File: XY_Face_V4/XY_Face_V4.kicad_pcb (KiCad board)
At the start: 4 copper layers, 83 x 98 mm, 38 parts, among them CN1 DF11-2DSA-4DP, J11 DF11-4DP-2DSA, J13 DF11-4DP-2DSA, J2 Conn_01x01, J3 Conn_01x01, J4 Conn_01x01, J5 Conn_01x01, Q2 CSD17576Q5B, U1 VEML7700, U2 TMP112xxDRL, U3 DRV2605LDGS, U4 TCA4311ADGKR, U5 5040500691, U6 5040500691

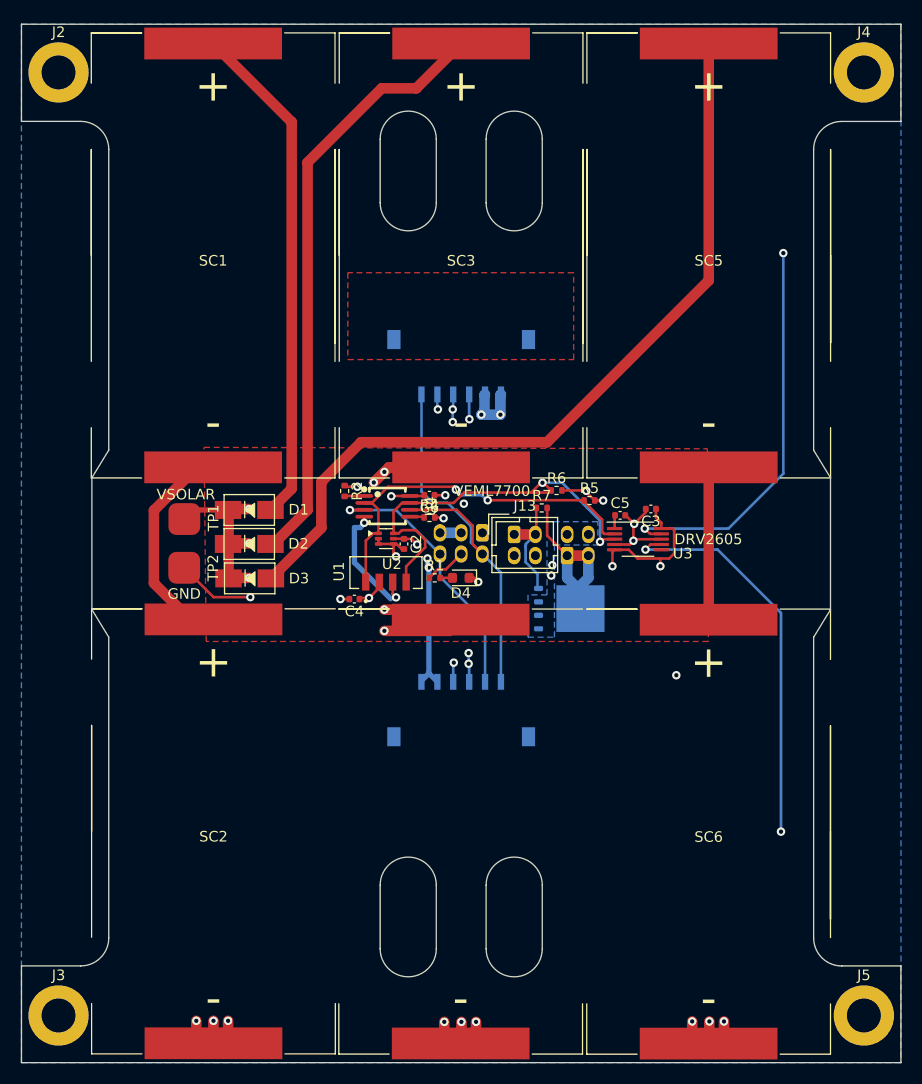
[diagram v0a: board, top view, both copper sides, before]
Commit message: Removed 2p Solar Cells
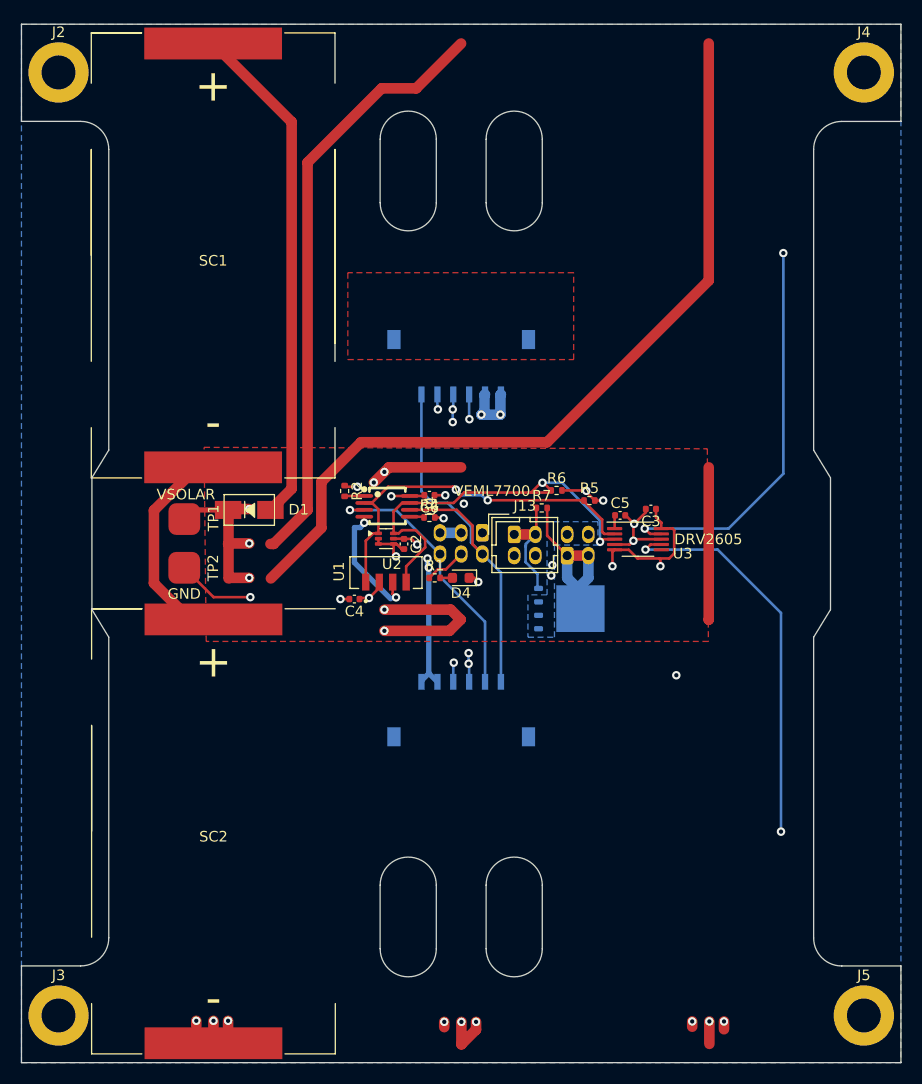
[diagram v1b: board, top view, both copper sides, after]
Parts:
- removed D2, D3: CDBA240LL-HF, SolarPanelBoards:DO-214AC
- removed SC3, SC4, SC5, SC6: SM101K07TF, SolarPanelBoards:KXOB101K08F-TR

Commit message: V4: Added new Cells to Footprint
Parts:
- removed U1: VEML7700, VEML7700-TT:XDCR_VEML7700-TT
- added U7: VEML6031X00, easyeda2kicad:SENSOR-SMD_VEML6031X00, F.Cu at (130.5, 116.0)
- SC1, SC2: value SM101K07TF -> SM261K10TF; footprint SolarPanelBoards:KXOB101K08F-TR -> Solar_Cell_Library:SM261K10TF
- moved SC1 23.4 mm to (144.4, 88.5), turned to 180 degrees
- moved SC2 23.3 mm to (144.4, 141.0), turned to 180 degrees
- moved U2 6.81 mm to (130.7, 113.0)
- moved C2 6.73 mm to (132.5, 113.5)
- moved TP1 4.40 mm to (114.0, 113.0)
- moved TP2 4.39 mm to (114.0, 116.5)
- moved C4 3.53 mm to (134.0, 116.5)
- moved D1 3.41 mm to (124.5, 115.0), turned to 180 degrees
- moved R7 2.96 mm to (155.0, 112.0)
- moved C3 0.50 mm to (162.4, 112.0)
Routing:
- net Net-(D3-A): track 77.9 -> 0.00 mm
- net Net-(SC1--): track 21.2 -> 82.5 mm
- net Net-(D2-A): track 56.8 -> 0.00 mm
- net Net-(SC3--): track 39.9 -> 0.00 mm, vias 4 -> 0
- net GND: track 53.5 -> 26.9 mm, vias 21 -> 9
- net Net-(D1-A): track 47.9 -> 26.5 mm
- net Net-(SC5--): track 14.4 -> 0.00 mm
- net /SDA: track 39.0 -> 28.7 mm
- net VSOLAR: track 87.5 -> 77.6 mm, vias 7 -> 4
- net /SCL: track 36.0 -> 28.4 mm
- net Net-(J13-Pin_1): track 10.5 -> 11.8 mm
- net /RBF_High: track 18.1 -> 17.1 mm
- net +3V3: track 105.9 -> 105.3 mm, vias 13 -> 12
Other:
- board text removed: "VEML7700"

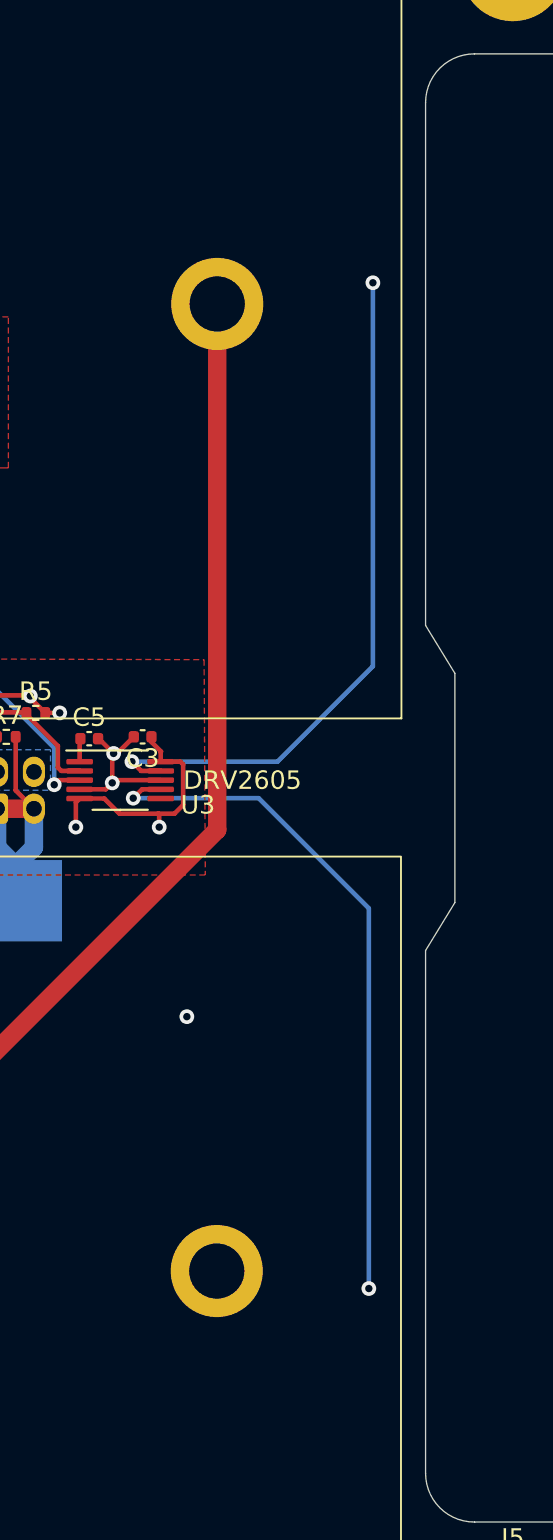
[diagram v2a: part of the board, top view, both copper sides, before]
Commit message: V4: Fixed In1 Coils
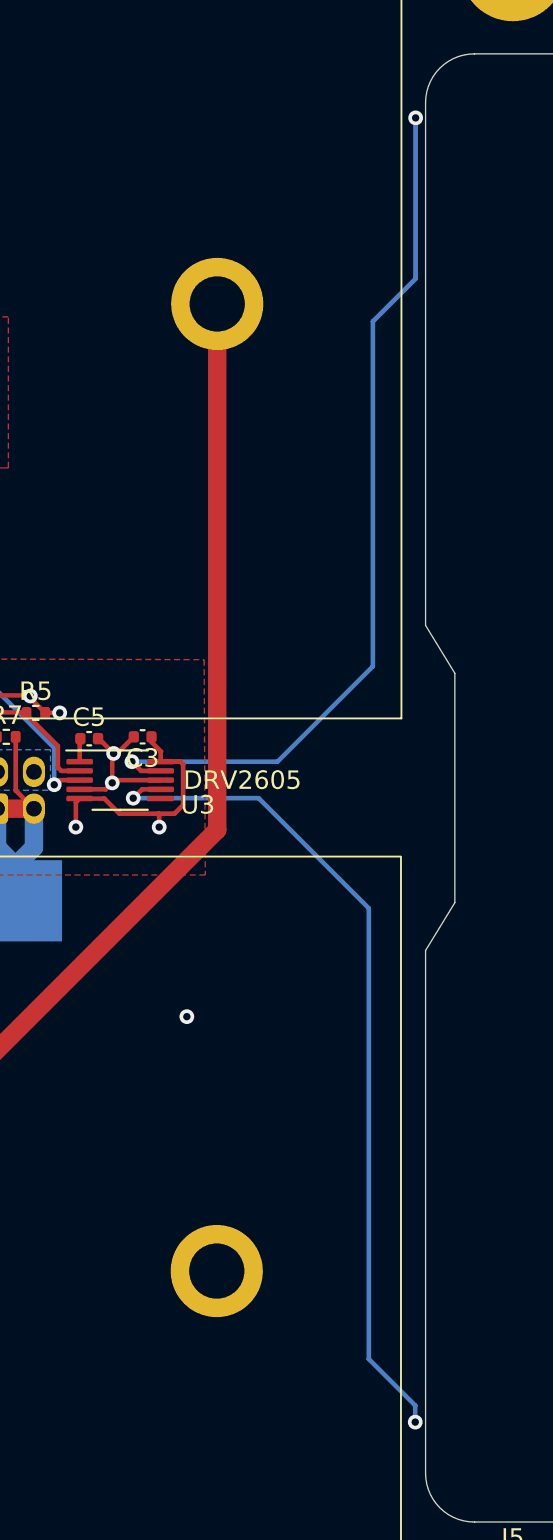
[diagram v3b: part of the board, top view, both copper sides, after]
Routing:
- net Net-(U3-OUT+): track 9246.2 -> 9743.8 mm

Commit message: V4: Completed Redraw of Traces
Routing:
- net Net-(U3-OUT+): track 9743.8 -> 10520.8 mm

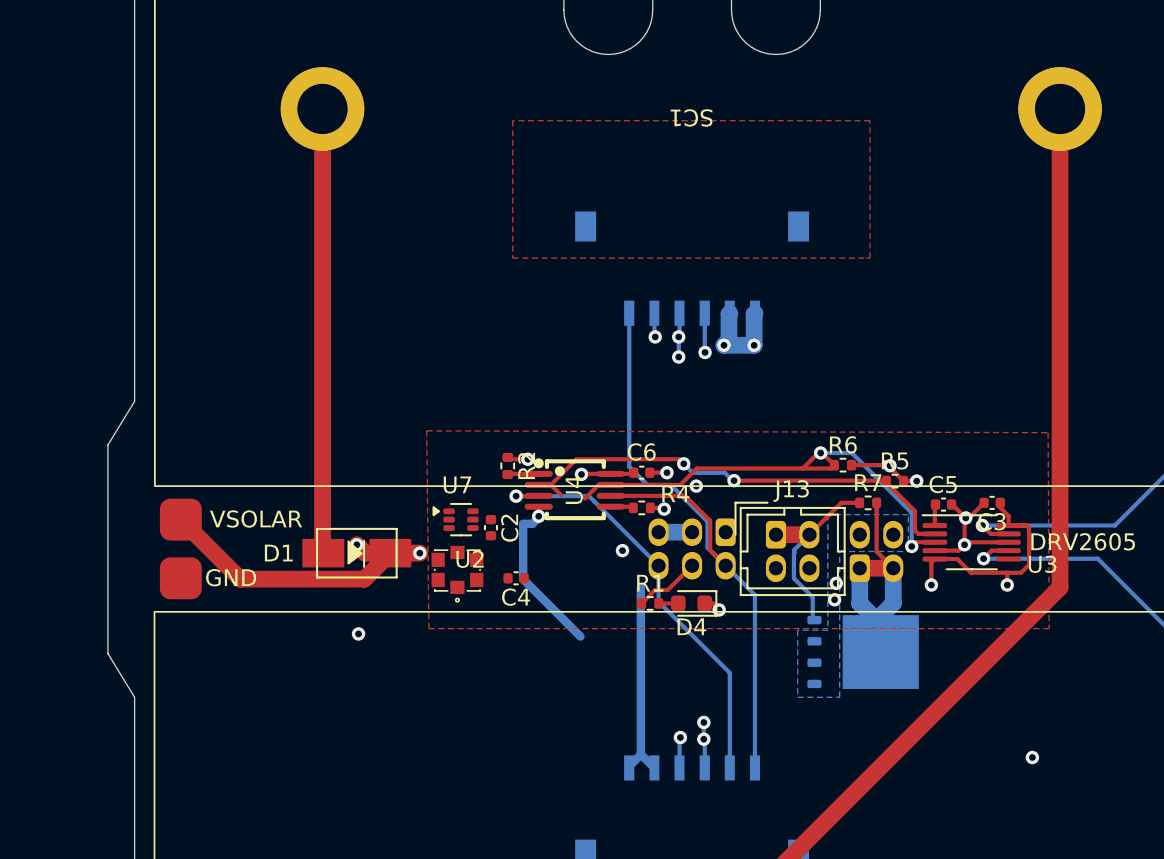
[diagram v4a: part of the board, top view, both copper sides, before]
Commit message: V4: Finished Layout Update for New Cells
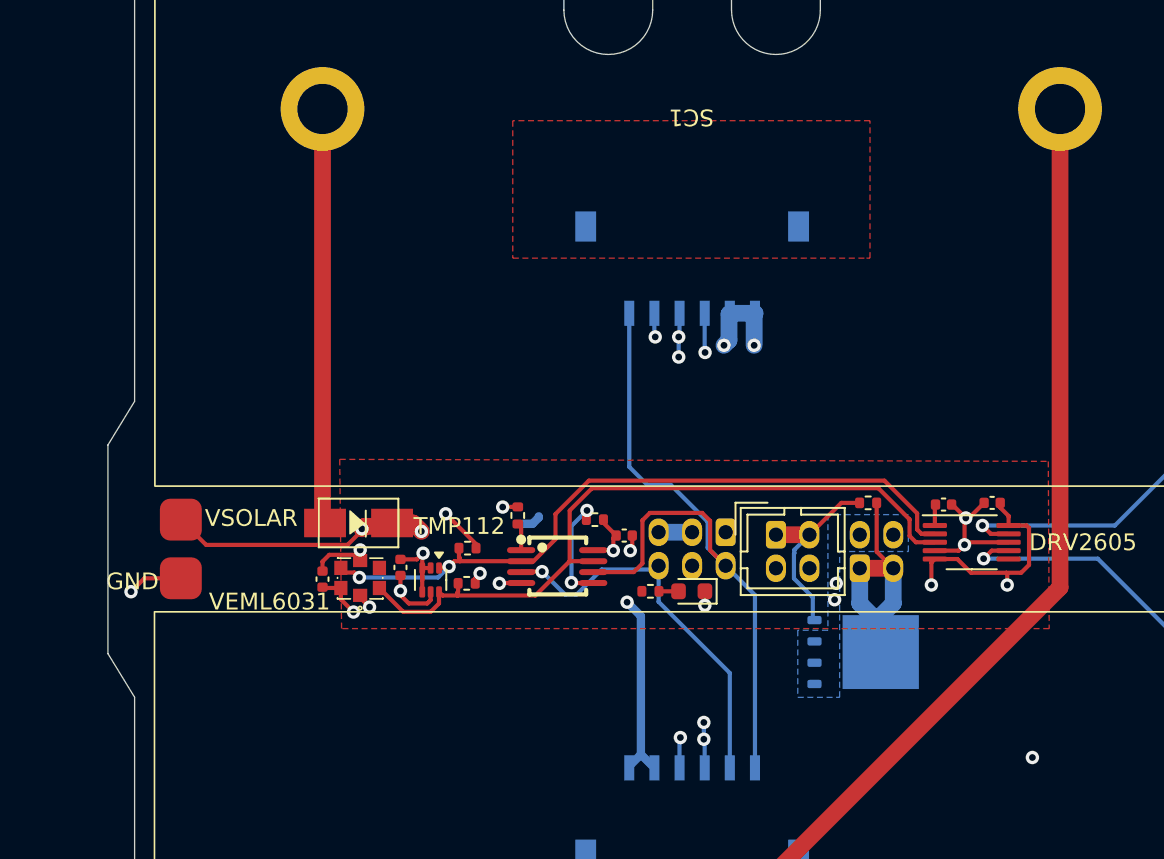
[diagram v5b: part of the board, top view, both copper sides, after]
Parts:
- moved R5 25.8 mm to (131.1, 114.7)
- moved R6 23.5 mm to (131.1, 116.8)
- moved C4 11.6 mm to (122.5, 116.5), turned to 90 degrees
- moved C2 5.90 mm to (127.1, 115.8), turned to 90 degrees
- moved U7 5.82 mm to (124.7, 116.5)
- moved U4 4.67 mm to (136.4, 115.8)
- moved U2 4.03 mm to (128.9, 116.6), turned to -90 degrees
- moved C6 3.89 mm to (140.4, 114.0)
- moved R2 3.01 mm to (134.1, 112.8)
- moved R4 2.89 mm to (138.7, 113.0)
- moved D1 1.80 mm to (124.6, 113.2)
- moved D4 0.73 mm to (144.5, 117.3)
- moved R1 0.73 mm to (142.0, 117.3)
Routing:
- net /SDA: track 28.7 -> 43.2 mm, vias 2 -> 0
- net /SCL: track 28.4 -> 42.1 mm
- net GND: track 26.9 -> 32.3 mm, vias 9 -> 11
- net Net-(U4-READY): track 1.37 -> 6.56 mm, vias 0 -> 2
- net VSOLAR: track 77.6 -> 81.8 mm, vias 4 -> 5
- net SDAIN: track 40.6 -> 44.2 mm
- net Net-(D1-A): track 26.5 -> 25.0 mm
- net SCLIN: track 46.8 -> 45.4 mm
- net +3V3: track 105.3 -> 106.7 mm
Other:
- board text added: "TMP112"
- board text added: "VEML6031"
